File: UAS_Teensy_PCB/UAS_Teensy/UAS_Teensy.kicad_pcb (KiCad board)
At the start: 2 copper layers, 2 parts

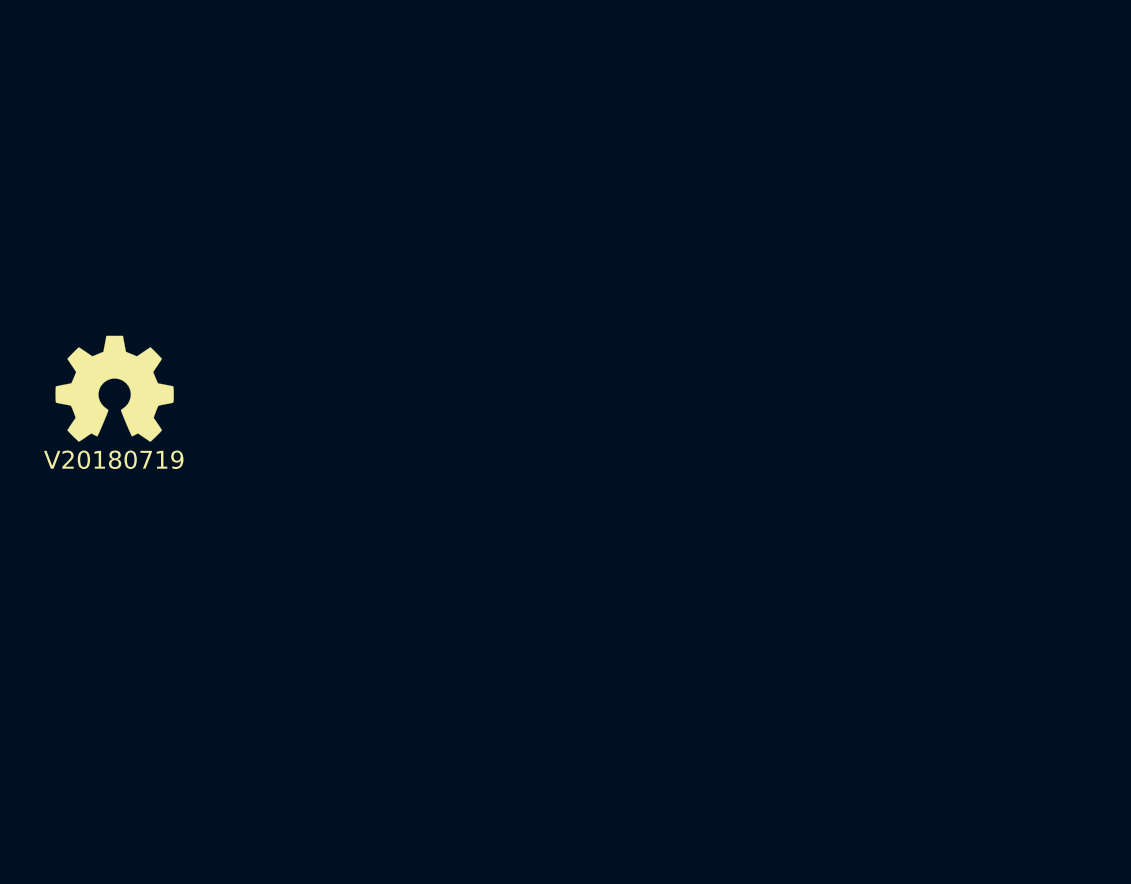
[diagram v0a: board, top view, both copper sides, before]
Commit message: Teensy Board Prep V1.1
Updated the Teensy Footprint/Symbol to match. Added entire Teensy library in case we just decided to use a Teensy 1.0 #businessMindset
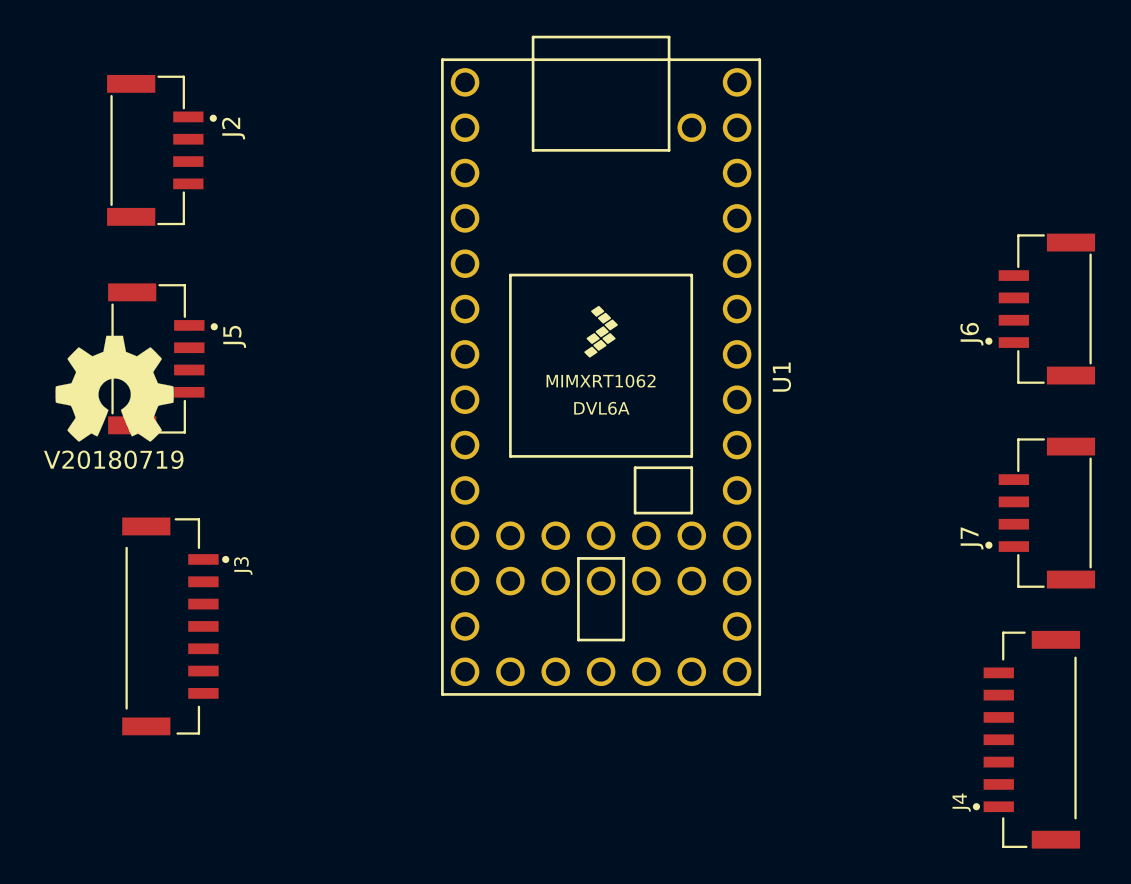
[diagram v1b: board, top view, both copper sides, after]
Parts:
- added J2: SM04B-GHS-TB(LF)(SN)-, UAS_Teensy:JST_SM04B-GHS-TB(LF)(SN)-, F.Cu at (149.9, 87.6)
- added J3: SM07B-GHS-TB(LF)(SN), UAS_Teensy:JST_SM07B-GHS-TB(LF)(SN), F.Cu at (151.1, 114.3)
- added J4: SM07B-GHS-TB(LF)(SN), UAS_Teensy:JST_SM07B-GHS-TB(LF)(SN), F.Cu at (199.4, 120.7)
- added J5: SM04B-GHS-TB(LF)(SN)-, UAS_Teensy:JST_SM04B-GHS-TB(LF)(SN)-, F.Cu at (149.9, 99.3)
- added J6: SM04B-GHS-TB(LF)(SN)-, UAS_Teensy:JST_SM04B-GHS-TB(LF)(SN)-, F.Cu at (200.7, 96.5)
- added J7: SM04B-GHS-TB(LF)(SN)-, UAS_Teensy:JST_SM04B-GHS-TB(LF)(SN)-, F.Cu at (200.7, 108.0)
- added U1: Teensy4.0, UAS_Teensy:Teensy40, F.Cu at (175.3, 100.3)

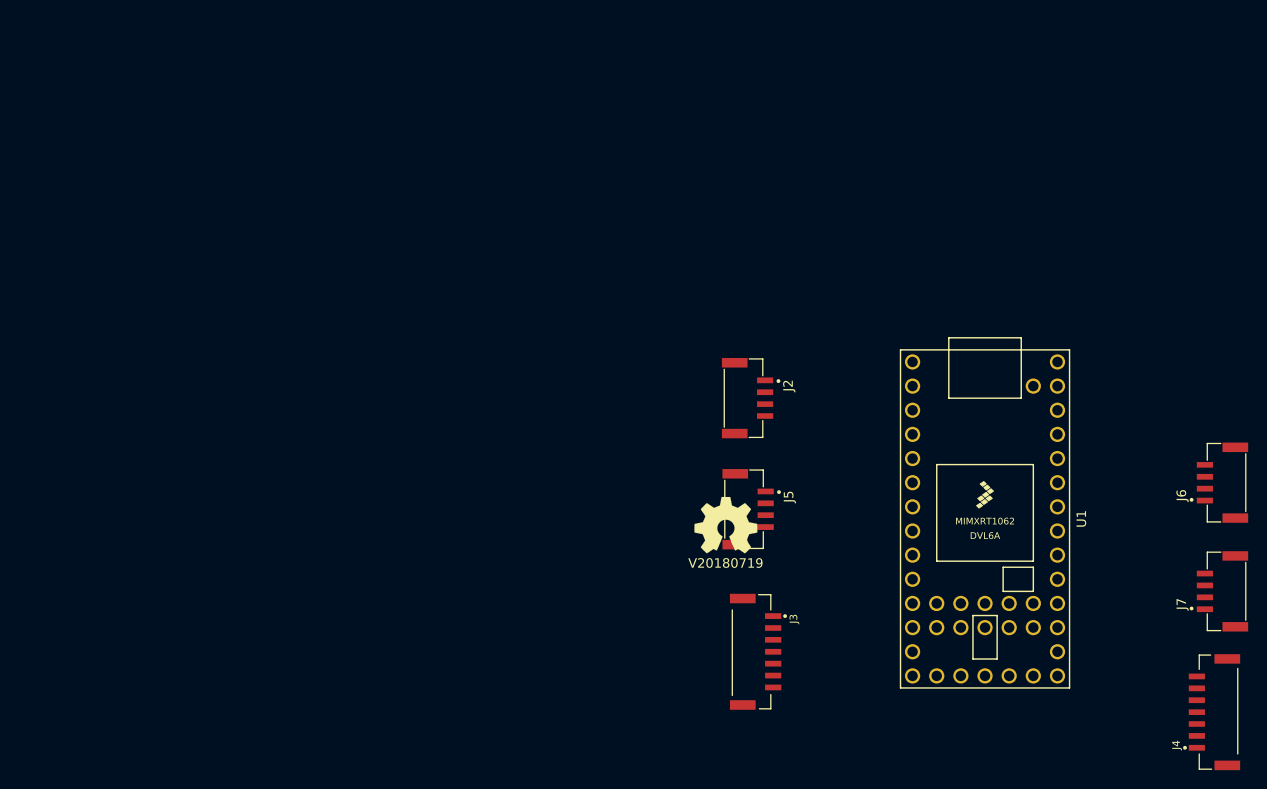
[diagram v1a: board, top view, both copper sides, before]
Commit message: pcb dxf updates
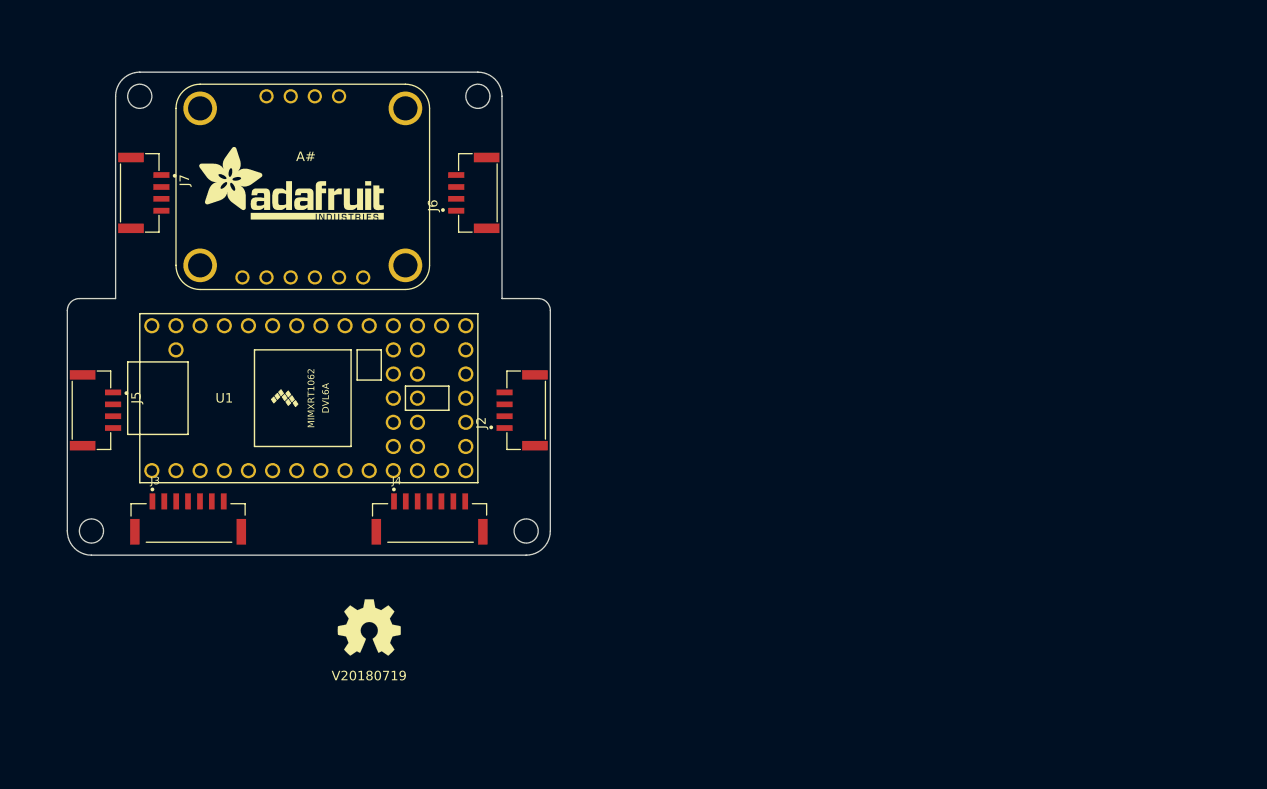
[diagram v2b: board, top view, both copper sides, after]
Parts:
- added A#: BNO055_Breakout, UAS_Teensy:BNO055_Breakout, F.Cu at (116.8, 54.6)
- moved J7 121.7 mm to (86.4, 66.0), turned to 270 degrees
- moved J4 85.0 mm to (116.8, 100.3), turned to 0 degrees
- moved J6 84.4 mm to (121.9, 66.0)
- moved U1 72.2 mm to (104.1, 87.6), turned to 0 degrees
- moved J5 69.4 mm to (81.3, 88.9)
- moved J3 61.3 mm to (91.4, 100.3), turned to 0 degrees
- moved N1 39.0 mm to (110.5, 111.8)
- moved J2 22.9 mm to (127.0, 88.9), turned to 90 degrees
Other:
- board outline added: 50.8 x 50.8 mm

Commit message: Schematic Wiring V1
First Step in Schematic Wiring
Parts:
- removed A#: BNO055_Breakout, UAS_Teensy:BNO055_Breakout
- added J1: UAS-rescue_SM02B-PASS-TBT(LF)(SN)-SM02B-PASS-TBT_LF__SN_, UAS_Teensy:SM02BGHSTBLFSN, F.Cu at (127.0, 83.8)
- added U2: BNO055, UAS_Teensy:BNO055_Breakout, F.Cu at (118.1, 55.9)
- moved J4 6.35 mm to (110.5, 100.3)
- moved J2 5.08 mm to (127.0, 94.0)
- moved J3 3.81 mm to (95.2, 100.3)
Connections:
- J4 pad 1: Net-(J4-Pad1) -> Net-(J3-Pad1)
- U1 pad 1: Net-(U1-Pad1) -> Net-(J3-Pad1)
- U1 pad 10: Net-(U1-Pad10) -> Net-(J4-Pad4)
- U1 pad 11: Net-(U1-Pad11) -> Net-(J4-Pad5)
- U1 pad 12: Net-(U1-Pad12) -> Net-(J4-Pad6)
- U1 pad 13: Net-(U1-Pad13) -> Net-(J4-Pad7)
- U1 pad 2: Net-(U1-Pad2) -> Net-(J3-Pad2)
- U1 pad 3: Net-(U1-Pad3) -> Net-(J3-Pad3)
- U1 pad 4: Net-(U1-Pad4) -> Net-(J3-Pad4)
- U1 pad 5: Net-(U1-Pad5) -> Net-(J3-Pad5)
- U1 pad 6: Net-(U1-Pad6) -> Net-(J3-Pad6)
- U1 pad 7: Net-(U1-Pad7) -> Net-(J3-Pad7)
- U1 pad 8: Net-(U1-Pad8) -> Net-(J4-Pad2)
- U1 pad 9: Net-(U1-Pad9) -> Net-(J4-Pad3)
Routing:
- net Net-(J4-Pad7): track 0.00 -> 5.21 mm
- net Net-(J3-Pad7): track 0.00 -> 5.21 mm
- net Net-(J3-Pad1): track 0.00 -> 5.21 mm
- net Net-(J4-Pad6): track 0.00 -> 4.91 mm
- net Net-(J4-Pad2): track 0.00 -> 4.30 mm
- net Net-(J3-Pad6): track 0.00 -> 4.30 mm
- net Net-(J3-Pad2): track 0.00 -> 4.30 mm
- net Net-(J1-Pad1): track 0.00 -> 4.27 mm
- net Net-(J1-Pad2): track 0.00 -> 4.27 mm
- net Net-(J4-Pad5): track 0.00 -> 3.76 mm
- net Net-(J3-Pad5): track 0.00 -> 3.76 mm
- net Net-(J3-Pad3): track 0.00 -> 3.76 mm
- net Net-(J4-Pad3): track 0.00 -> 3.76 mm
- net Net-(J4-Pad4): track 0.00 -> 3.23 mm
- net Net-(J3-Pad4): track 0.00 -> 3.23 mm

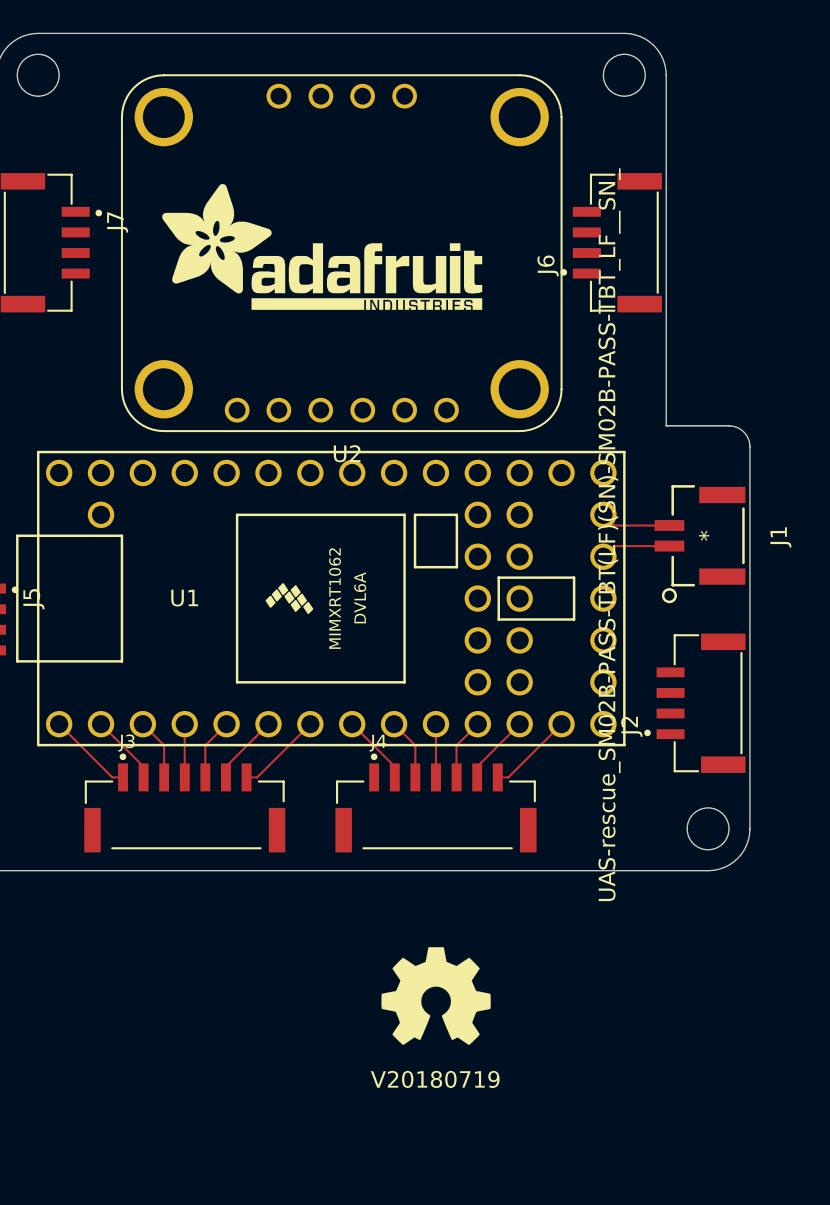
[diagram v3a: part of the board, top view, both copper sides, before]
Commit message: Teensy PCB Ready To Wire Up Update
Schematic is finalized and all that's left is to lay traces
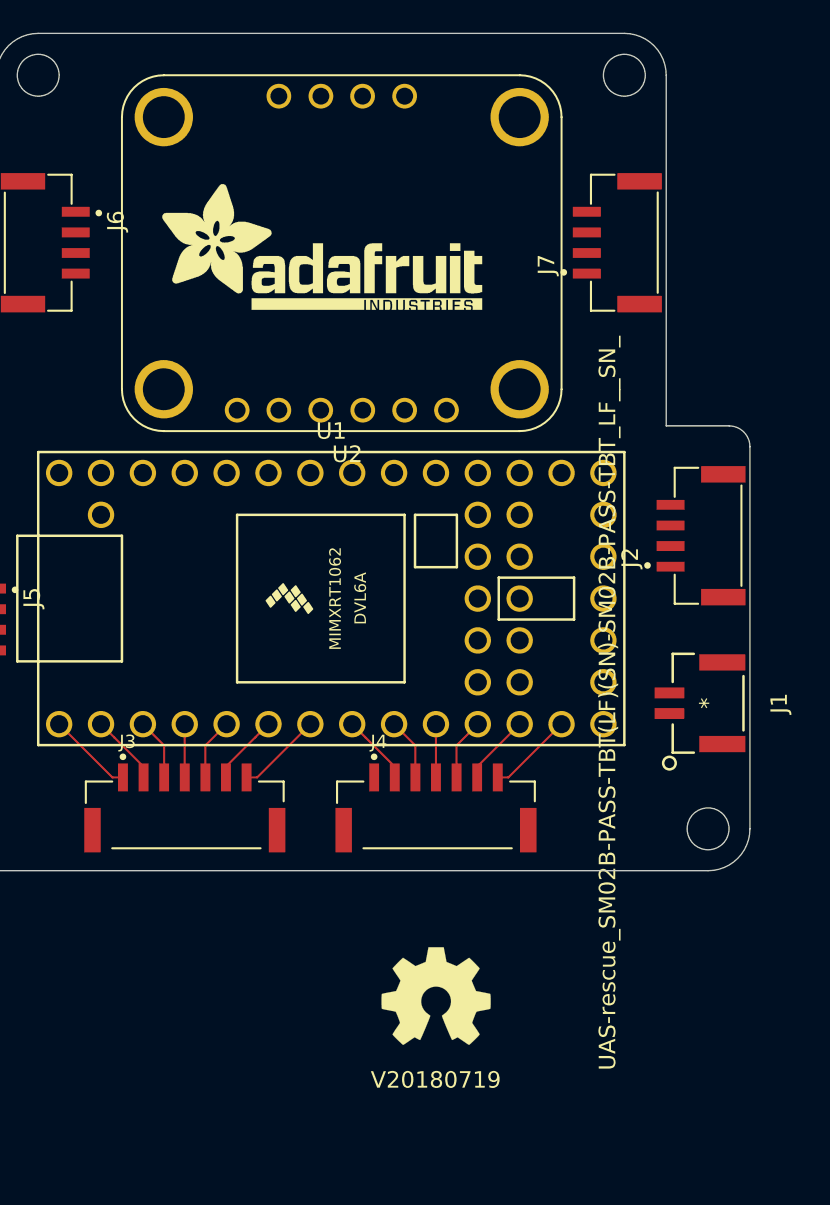
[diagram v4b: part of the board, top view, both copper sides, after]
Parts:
- moved J6 35.6 mm to (86.4, 66.0), turned to 270 degrees
- moved J7 35.6 mm to (121.9, 66.0), turned to 90 degrees
- moved J1 10.2 mm to (127.0, 94.0)
- moved J2 10.2 mm to (127.0, 83.8)
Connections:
- J2 pad 3: Net-(J2-Pad3) -> GND
- J2 pad 4: Net-(J2-Pad4) -> 5V
- J3 pad 1: Net-(J3-Pad1) -> GND
- J4 pad 1: Net-(J3-Pad1) -> GND
- J5 pad 3: Net-(J5-Pad3) -> GND
- J5 pad 4: Net-(J5-Pad4) -> 5V
- J6 pad 3: Net-(J6-Pad3) -> GND
- J6 pad 4: Net-(J6-Pad4) -> 5V
- J7 pad 3: Net-(J7-Pad3) -> GND
- J7 pad 4: Net-(J7-Pad4) -> 5V
- U1 pad 1: Net-(J3-Pad1) -> GND
- U1 pad 14: Net-(U1-Pad14) -> Net-(J2-Pad2)
- U1 pad 18: Net-(J1-Pad1) -> Net-(U1-Pad18)
- U1 pad 19: Net-(J1-Pad2) -> Net-(U1-Pad19)
- U1 pad 20: Net-(U1-Pad20) -> Net-(J2-Pad1)
- U1 pad 21: Net-(U1-Pad21) -> Net-(J5-Pad1)
- U1 pad 22: Net-(U1-Pad22) -> Net-(J5-Pad2)
- U1 pad 29: Net-(U1-Pad29) -> Net-(J6-Pad1)
- U1 pad 30: Net-(U1-Pad30) -> Net-(J6-Pad2)
- U1 pad 32: Net-(U1-Pad32) -> GND
- U1 pad 33: Net-(U1-Pad33) -> 5V
- U1 pad 35: Net-(U1-Pad35) -> Net-(J7-Pad2)
- U1 pad 36: Net-(U1-Pad36) -> Net-(J7-Pad1)
- U1 pad 40: Net-(U1-Pad40) -> Net-(J1-Pad2)
- U1 pad 44: Net-(U1-Pad44) -> Net-(J1-Pad1)
- U2 pad 12: (no net) -> Net-(U1-Pad25)
- U2 pad 13: (no net) -> Net-(U1-Pad26)
- U2 pad 4: Net-(U2-Pad4) -> (no net)
- U2 pad 5: Net-(U2-Pad5) -> (no net)
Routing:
- net Net-(J3-Pad1): track 5.21 -> 0.00 mm
- net GND: track 0.00 -> 5.21 mm
- net Net-(J1-Pad1): track 4.27 -> 0.00 mm
- net Net-(J1-Pad2): track 4.27 -> 0.00 mm

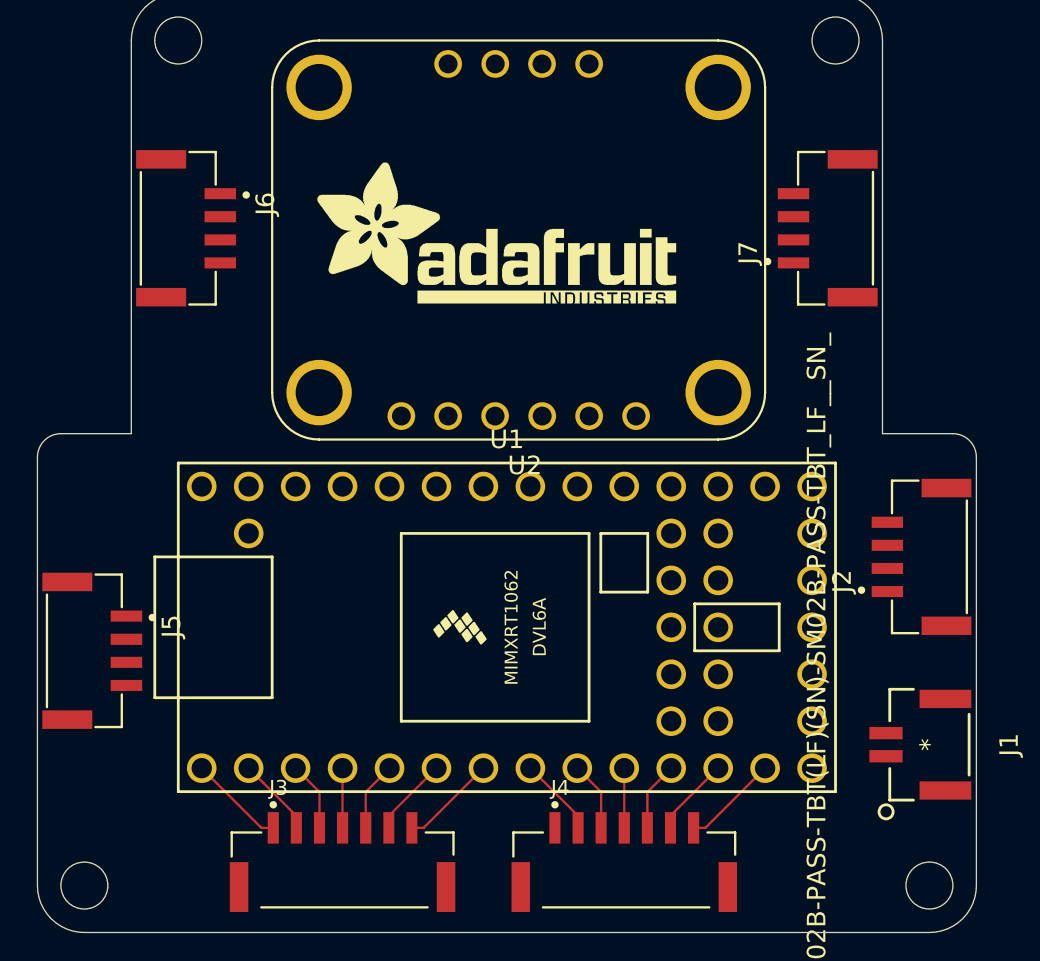
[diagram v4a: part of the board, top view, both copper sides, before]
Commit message: Teensy PCB Finished, Validation Next
Teensy PCB is done, just need to validate the board design and order.
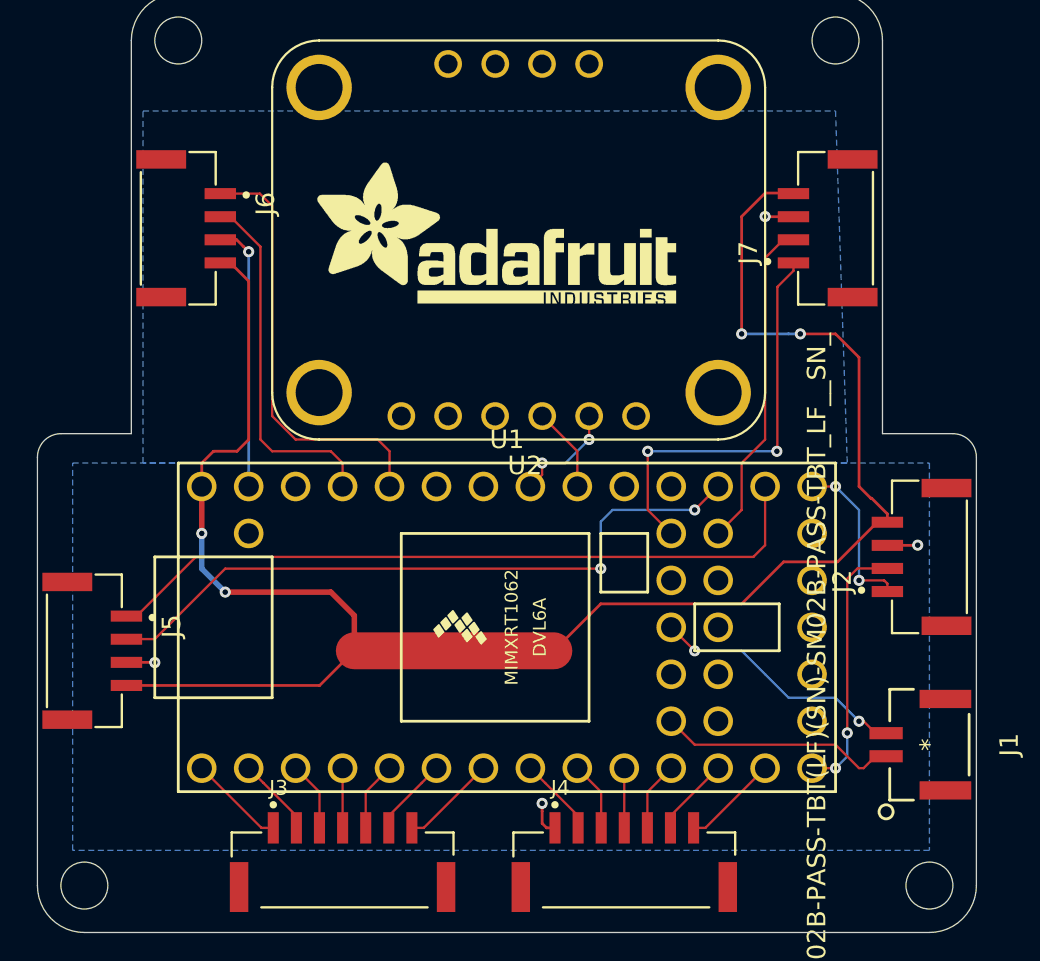
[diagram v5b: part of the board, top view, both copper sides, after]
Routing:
- net 5V: track 0.00 -> 101.5 mm, vias 0 -> 4
- net Net-(J5-Pad1): track 0.00 -> 39.3 mm
- net Net-(J5-Pad2): track 0.00 -> 36.9 mm, vias 0 -> 2
- net Net-(J6-Pad1): track 0.00 -> 24.1 mm
- net Net-(J7-Pad1): track 0.00 -> 22.5 mm, vias 0 -> 2
- net GND: track 5.21 -> 26.3 mm, vias 0 -> 5
- net Net-(J6-Pad2): track 0.00 -> 19.5 mm
- net Net-(J7-Pad2): track 0.00 -> 17.9 mm
- net Net-(J2-Pad2): track 0.00 -> 14.2 mm, vias 0 -> 2
- net Net-(J1-Pad2): track 0.00 -> 14.0 mm, vias 0 -> 2
- net Net-(J1-Pad1): track 0.00 -> 12.9 mm
- net Net-(J2-Pad1): track 0.00 -> 8.91 mm, vias 0 -> 2
- net Net-(U1-Pad26): track 0.00 -> 5.87 mm, vias 0 -> 2
- net Net-(U1-Pad25): track 0.00 -> 4.60 mm
- added copper zone on B.Cu, net GND
